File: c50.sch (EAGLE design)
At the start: 15 parts, among them IC1 7805TV, IC2 UA555N

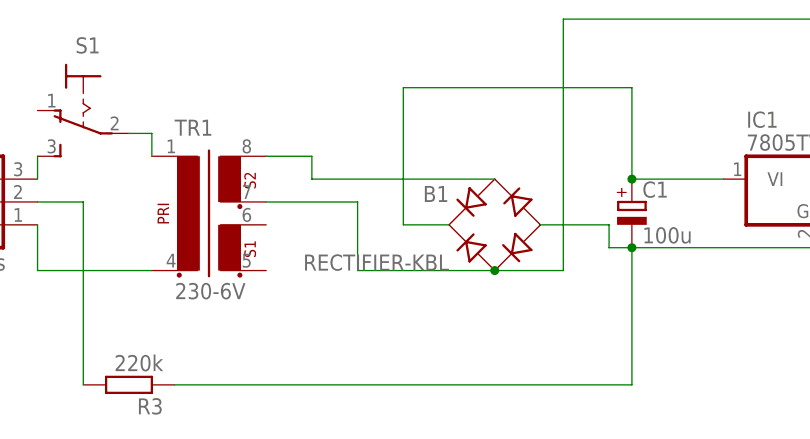
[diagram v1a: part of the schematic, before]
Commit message: Modified gerbers, sistemati drill e holes. Routing da finire.
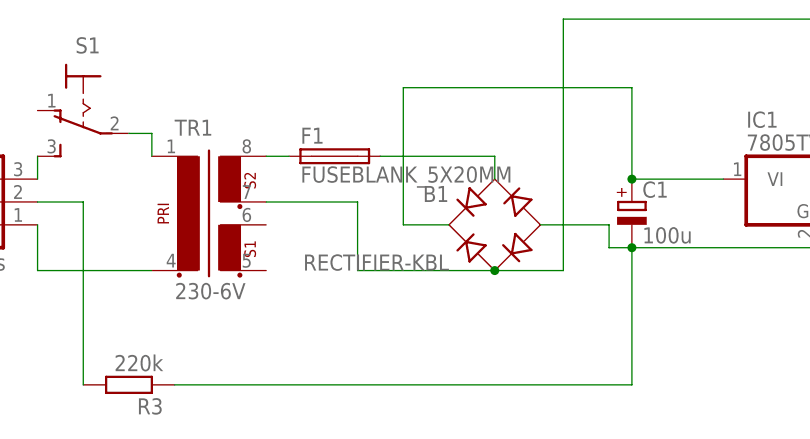
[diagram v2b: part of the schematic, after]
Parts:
- added F1: FUSEBLANK_5X20MM, fuse:FUSEBLANK_5X20MM
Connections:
- new net N$13: B1.AC1, F1.2
- net N$6: now also F1.1; no longer B1.AC1
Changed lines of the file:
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@@
 <setting verticaltext="up"/>
 </settings>
-<grid distance="0.1" unitdist="inch" unit="inch" style="lines" multiple="1" display="no" altdistance="0.01" altunitdist="inch" altunit="inch"/>
+<grid distance="0.1" unitdist="inch" unit="inch" style="lines" multiple="1" display="yes" altdistance="0.01" altunitdist="inch" altunit="inch"/>
 <layers>
 <layer number="1" name="Top" color="4" fill="1" visible="no" active="no"/>
@@
 </variantdefs>
 <classes>
-<class number="0" name="default" width="0" drill="0">
+<class number="0" name="default" width="0.508" drill="0">
 </class>
 </classes>
@@
 <part name="JP1" library="SparkFun-Connectors" deviceset="M03" device="-SCREW-5MM" value="mains"/>
 <part name="S1" library="switch" deviceset="320-916" device=""/>
+<part name="F1" library="fuse" deviceset="FUSE" device="BLANK_5X20MM"/>
 </parts>
 <sheets>
@@
 <instance part="JP1" gate="G$1" x="-12.7" y="25.4"/>
 <instance part="S1" gate="1" x="0" y="35.56" rot="MR270"/>
+<instance part="F1" gate="G$1" x="27.94" y="30.48"/>
 </instances>
 <busses>
@@
 </segment>
 </net>
-<net name="N$6" class="0">
-<segment>
-<pinref part="B1" gate="1" pin="AC1"/>
-<wire x1="45.72" y1="27.94" x2="25.4" y2="27.94" width="0.1524" layer="91"/>
-<wire x1="25.4" y1="27.94" x2="25.4" y2="30.48" width="0.1524" layer="91"/>
-<pinref part="TR1" gate="1" pin="6"/>
-<wire x1="25.4" y1="30.48" x2="20.32" y2="30.48" width="0.1524" layer="91"/>
-</segment>
-</net>
 <net name="N$1" class="0">
 <segment>
@@
 </segment>
 </net>
+<net name="N$6" class="0">
+<segment>
+<pinref part="TR1" gate="1" pin="6"/>
+<pinref part="F1" gate="G$1" pin="1"/>
+<wire x1="22.86" y1="30.48" x2="20.32" y2="30.48" width="0.1524" layer="91"/>
+</segment>
+</net>
+<net name="N$13" class="0">
+<segment>
+<pinref part="F1" gate="G$1" pin="2"/>
+<pinref part="B1" gate="1" pin="AC1"/>
+<wire x1="33.02" y1="30.48" x2="45.72" y2="30.48" width="0.1524" layer="91"/>
+<wire x1="45.72" y1="30.48" x2="45.72" y2="27.94" width="0.1524" layer="91"/>
+</segment>
+</net>

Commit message: Finished (maybe)
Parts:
- C5: device rcl:C-EU025-025X050 -> resistor:C-EU050-024X044
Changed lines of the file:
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@@
 <grid distance="0.1" unitdist="inch" unit="inch" style="lines" multiple="1" display="yes" altdistance="0.01" altunitdist="inch" altunit="inch"/>
 <layers>
-<layer number="1" name="Top" color="4" fill="1" visible="no" active="no"/>
-<layer number="16" name="Bottom" color="1" fill="1" visible="no" active="no"/>
-<layer number="17" name="Pads" color="2" fill="1" visible="no" active="no"/>
-<layer number="18" name="Vias" color="2" fill="1" visible="no" active="no"/>
-<layer number="19" name="Unrouted" color="6" fill="1" visible="no" active="no"/>
-<layer number="20" name="Dimension" color="15" fill="1" visible="no" active="no"/>
-<layer number="21" name="tPlace" color="7" fill="1" visible="no" active="no"/>
-<layer number="22" name="bPlace" color="7" fill="1" visible="no" active="no"/>
-<layer number="23" name="tOrigins" color="15" fill="1" visible="no" active="no"/>
-<layer number="24" name="bOrigins" color="15" fill="1" visible="no" active="no"/>
-<layer number="25" name="tNames" color="7" fill="1" visible="no" active="no"/>
-<layer number="26" name="bNames" color="7" fill="1" visible="no" active="no"/>
-<layer number="27" name="tValues" color="7" fill="1" visible="no" active="no"/>
-<layer number="28" name="bValues" color="7" fill="1" visible="no" active="no"/>
+<layer number="1" name="Top" color="4" fill="1" visible="yes" active="no"/>
+<layer number="16" name="Bottom" color="1" fill="1" visible="yes" active="no"/>
+<layer number="17" name="Pads" color="2" fill="1" visible="yes" active="no"/>
+<layer number="18" name="Vias" color="2" fill="1" visible="yes" active="no"/>
+<layer number="19" name="Unrouted" color="6" fill="1" visible="yes" active="no"/>
+<layer number="20" name="Dimension" color="15" fill="1" visible="yes" active="no"/>
+<layer number="21" name="tPlace" color="7" fill="1" visible="yes" active="no"/>
+<layer number="22" name="bPlace" color="7" fill="1" visible="yes" active="no"/>
+<layer number="23" name="tOrigins" color="15" fill="1" visible="yes" active="no"/>
+<layer number="24" name="bOrigins" color="15" fill="1" visible="yes" active="no"/>
+<layer number="25" name="tNames" color="7" fill="1" visible="yes" active="no"/>
+<layer number="26" name="bNames" color="7" fill="1" visible="yes" active="no"/>
+<layer number="27" name="tValues" color="7" fill="1" visible="yes" active="no"/>
+<layer number="28" name="bValues" color="7" fill="1" visible="yes" active="no"/>
 <layer number="29" name="tStop" color="7" fill="3" visible="no" active="no"/>
 <layer number="30" name="bStop" color="7" fill="6" visible="no" active="no"/>
@@
 <layer number="35" name="tGlue" color="7" fill="4" visible="no" active="no"/>
 <layer number="36" name="bGlue" color="7" fill="5" visible="no" active="no"/>
-<layer number="37" name="tTest" color="7" fill="1" visible="no" active="no"/>
-<layer number="38" name="bTest" color="7" fill="1" visible="no" active="no"/>
+<layer number="37" name="tTest" color="7" fill="1" visible="yes" active="no"/>
+<layer number="38" name="bTest" color="7" fill="1" visible="yes" active="no"/>
 <layer number="39" name="tKeepout" color="4" fill="11" visible="no" active="no"/>
 <layer number="40" name="bKeepout" color="1" fill="11" visible="no" active="no"/>
@@
 <layer number="44" name="Drills" color="7" fill="1" visible="no" active="no"/>
 <layer number="45" name="Holes" color="7" fill="1" visible="no" active="no"/>
-<layer number="46" name="Milling" color="3" fill="1" visible="no" active="no"/>
-<layer number="47" name="Measures" color="7" fill="1" visible="no" active="no"/>
-<layer number="48" name="Document" color="7" fill="1" visible="no" active="no"/>
-<layer number="49" name="Reference" color="7" fill="1" visible="no" active="no"/>
-<layer number="50" name="dxf" color="7" fill="1" visible="no" active="no"/>
-<layer number="51" name="tDocu" color="7" fill="1" visible="no" active="no"/>
-<layer number="52" name="bDocu" color="7" fill="1" visible="no" active="no"/>
-<layer number="53" name="tGND_GNDA" color="7" fill="9" visible="no" active="no"/>
-<layer number="54" name="bGND_GNDA" color="1" fill="9" visible="no" active="no"/>
-<layer number="56" name="wert" color="7" fill="1" visible="no" active="no"/>
-<layer number="57" name="tCAD" color="7" fill="1" visible="no" active="no"/>
+<layer number="46" name="Milling" color="3" fill="1" visible="yes" active="no"/>
+<layer number="47" name="Measures" color="7" fill="1" visible="yes" active="no"/>
+<layer number="48" name="Document" color="7" fill="1" visible="yes" active="no"/>
+<layer number="49" name="Reference" color="7" fill="1" visible="yes" active="no"/>
+<layer number="50" name="dxf" color="7" fill="1" visible="yes" active="no"/>
+<layer number="51" name="tDocu" color="7" fill="1" visible="yes" active="no"/>
+<layer number="52" name="bDocu" color="7" fill="1" visible="yes" active="no"/>
+<layer number="53" name="tGND_GNDA" color="7" fill="9" visible="yes" active="no"/>
+<layer number="54" name="bGND_GNDA" color="1" fill="9" visible="yes" active="no"/>
+<layer number="56" name="wert" color="7" fill="1" visible="yes" active="no"/>
+<layer number="57" name="tCAD" color="7" fill="1" visible="yes" active="no"/>
 <layer number="90" name="Modules" color="5" fill="1" visible="yes" active="yes"/>
 <layer number="91" name="Nets" color="2" fill="1" visible="yes" active="yes"/>
@@
 <class number="0" name="default" width="0.508" drill="0">
 </class>
+<class number="1" name="mask" width="0" drill="0">
+<clearance class="0" value="0.254"/>
+</class>
+<class number="2" name="ground" width="1.016" drill="0.9906">
+</class>
 </classes>
 <parts>
@@
 <part name="C3" library="resistor" deviceset="C-EU" device="050-024X044" value="100n"/>
 <part name="R1" library="resistor" deviceset="R-EU_" device="0207/10" value="100R"/>
-<part name="C5" library="rcl" deviceset="C-EU" device="025-025X050" value="10n"/>
+<part name="C5" library="resistor" deviceset="C-EU" device="050-024X044" value="10n"/>
 <part name="C4" library="rcl" deviceset="CPOL-EU" device="E5-13" value="32u"/>
 <part name="C1" library="rcl" deviceset="CPOL-EU" device="E2.5-7" value="100u"/>
@@
 </busses>
 <nets>
-<net name="GND" class="0">
+<net name="GND" class="2">
 <segment>
 <pinref part="B1" gate="1" pin="-"/>
